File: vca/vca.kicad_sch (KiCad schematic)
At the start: 16 parts

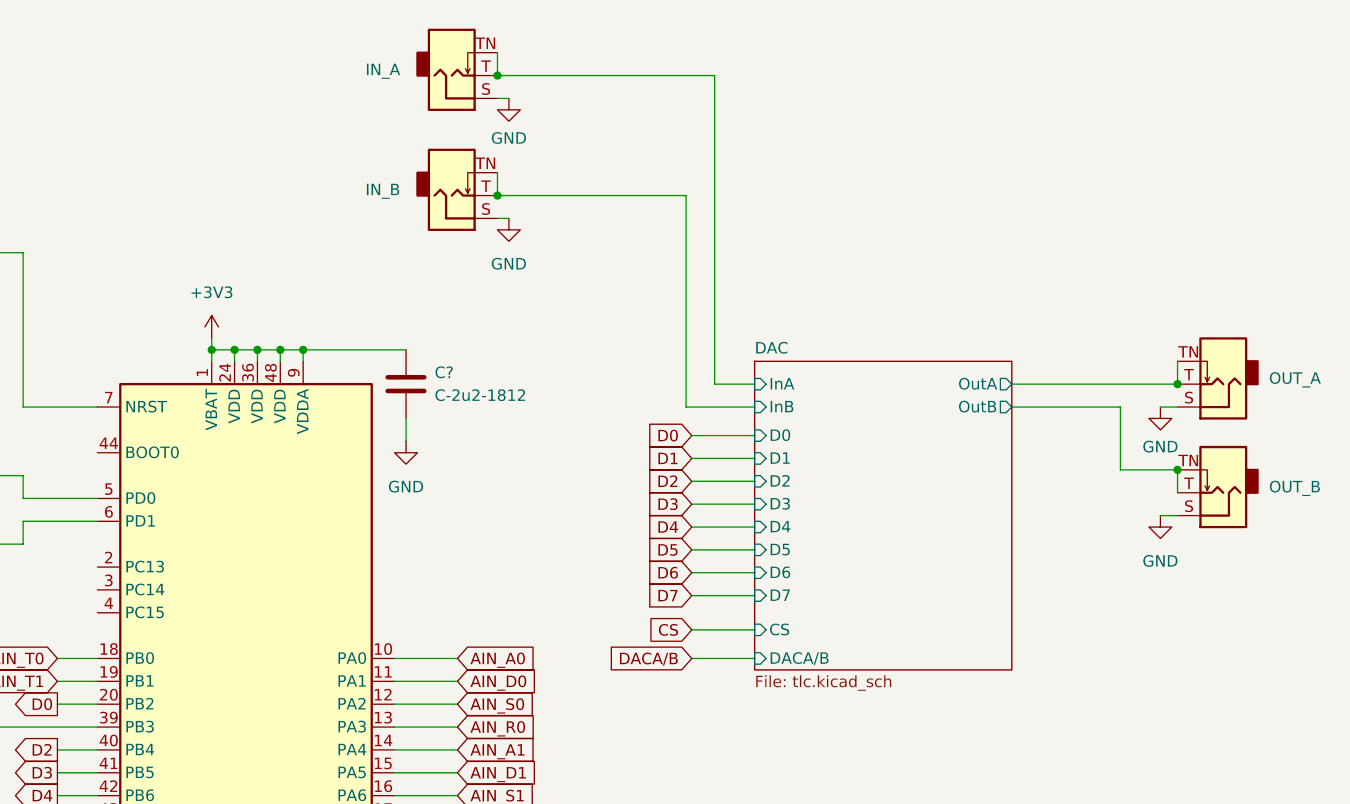
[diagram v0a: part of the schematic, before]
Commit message: added LEDs to LUM
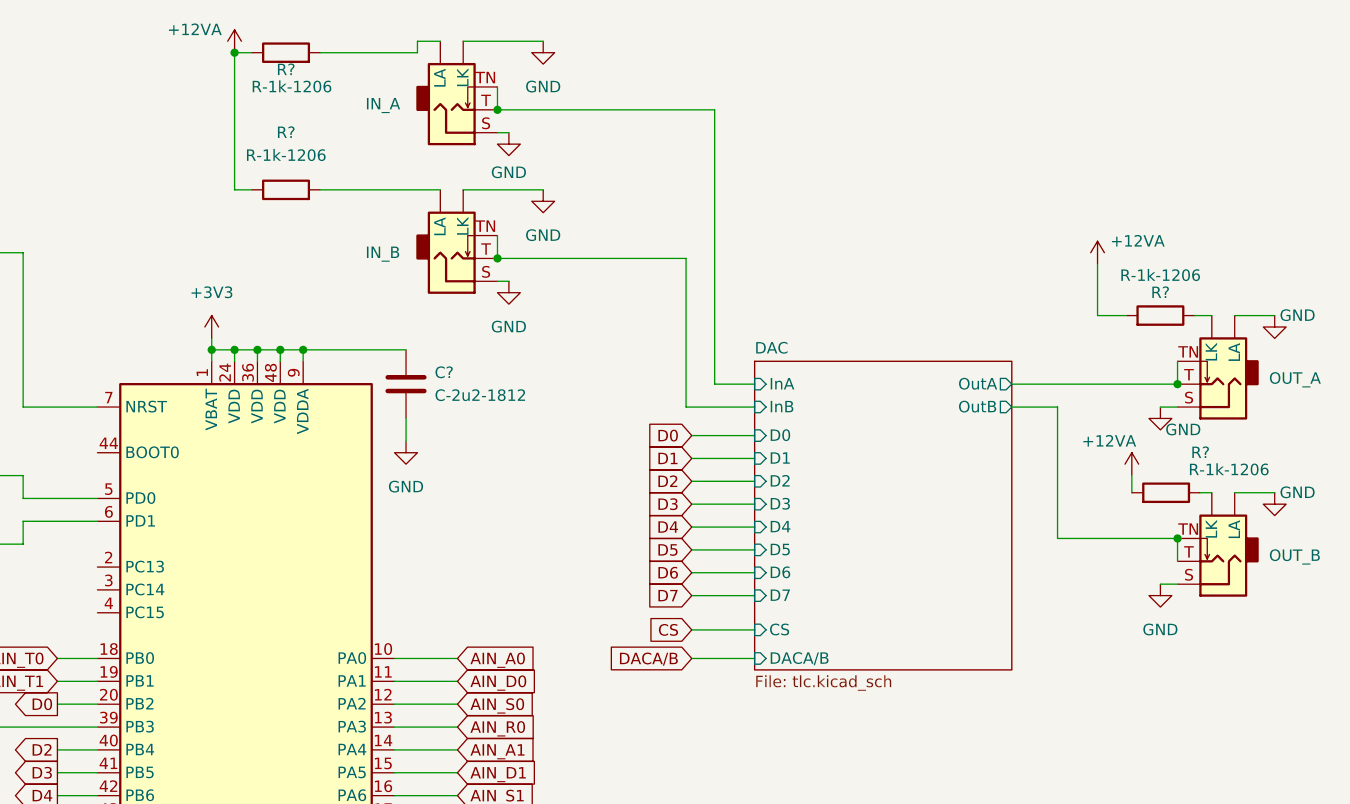
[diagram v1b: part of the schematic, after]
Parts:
- added R? (x4): R-1k-1206, Resistor_SMD:R_1206_3216Metric_Pad1.30x1.75mm_HandSolder, symbol eurorack:R-1k-1206
- IN_A, IN_B, OUT_A, OUT_B: footprint eurorack:LUM 1502-03 -> eurorack:LUM 1502-03 LED; symbol eurorack:LUM-1502-03_3.5mm_mono_vertical_jack -> eurorack:LUM-1502-03_3.5mm_mono_vertical_jack_LED
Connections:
- net GND: now also IN_A. (LK), IN_B. (LK), OUT_A. (LK), OUT_B. (LK)
- new net: OUT_B. (LK), R?.1
- new net: IN_B. (LK), R?.2
- new net: IN_A. (LK), R?.2
- new net: OUT_A. (LK), R?.1
- new net +12VA: R?.1, R?.1, R?.2, R?.2

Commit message: some fixes, starting to work on PCB
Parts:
- gave numbers to parts that had none: 16
- renumbered IN_A to IN_A1, IN_B to IN_B1, OUT_A to OUT_A1, OUT_B to OUT_B1
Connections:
- net DAC/InA: no longer IN_A1.TN
- net DAC/InB: no longer IN_B1.TN
- net GND: now also IN_A1.LK, IN_B1.LK, OUT_A1.LA, OUT_B1.LA; no longer IN_A1. (LK), IN_B1. (LK), OUT_A1. (LK), OUT_B1. (LK)
- net at R6.1: now also OUT_B1.LK; no longer OUT_B1. (LK)
- net at R4.2: now also IN_B1.LA; no longer IN_B1. (LK)
- net at R3.2: now also IN_A1.LA; no longer IN_A1. (LK)
- net at R5.1: now also OUT_A1.LK; no longer OUT_A1. (LK)
- new net +10V: IN_A1.TN

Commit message: working on the PCB
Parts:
- added CON_BACK1, CON_FRONT1: 2_15_Back_Front_Conn_70, eurorack:2_15_back_front_conn_70, symbol eurorack:2_15_Back_Front_Conn_70
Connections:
- net +10V: now also IN_B1.TN
- net AIN_A0 renamed B_AIN_A0
- net AIN_A0_LED renamed B_AIN_A0_LED
- net AIN_A1 renamed B_AIN_A1
- net AIN_A1_LED renamed B_AIN_A1_LED
- net AIN_D0 renamed B_AIN_D0
- net AIN_D0_LED renamed B_AIN_D0_LED
- net AIN_D1 renamed B_AIN_D1
- net AIN_D1_LED renamed B_AIN_D1_LED
- net AIN_R0 renamed B_AIN_R0
- net AIN_R0_LED renamed B_AIN_R0_LED
- net AIN_R1 renamed B_AIN_R1
- net AIN_R1_LED renamed B_AIN_R1_LED
- net AIN_S0 renamed B_AIN_S0
- net AIN_S0_LED renamed B_AIN_S0_LED
- net AIN_S1 renamed B_AIN_S1
- net AIN_S1_LED renamed B_AIN_S1_LED
- net AIN_T0 renamed B_AIN_T0
- net AIN_T0_LED renamed B_AIN_T0_LED
- net AIN_T1 renamed B_AIN_T1
- net AIN_T1_LED renamed B_AIN_T1_LED
- net DAC/InA renamed F_INA
- net DAC/InB renamed F_INB
- net DAC/OutA renamed F_OUTA
- net DAC/OutB renamed F_OUTB
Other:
- moved on the sheet: C4, C5, C6, C7, IN_A1, IN_B1, OUT_A1, OUT_B1, R3, R4, R5, R6

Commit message: working on front panel
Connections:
- net +10V: now also CON_FRONT1.16
- net +12VA: now also CON_FRONT1.18
- net B_AIN_R0: now also CON_BACK1.21
- net B_AIN_R0_LED: now also CON_BACK1.20
- net B_INA: now also CON_BACK1.17
- net B_INB: now also CON_BACK1.26
- net B_OUTA: now also CON_BACK1.19
- net B_OUTB: now also CON_BACK1.30
- net F_INA: now also CON_FRONT1.17
- net F_INB: now also CON_FRONT1.26
- net F_OUTA: now also CON_FRONT1.19
- net F_OUTB: now also CON_FRONT1.30
- net GND: now also OUT_A1.LK, OUT_B1.LK; no longer OUT_A1.LA, OUT_B1.LA
- net at R6.1: now also OUT_B1.LA; no longer OUT_B1.LK
- net B_+10V: now reaches CON_BACK1.16
- net +12V: now reaches CON_BACK1.18
- net at R5.1: now also OUT_A1.LA; no longer OUT_A1.LK
- net F_AIN_R0_LED: now reaches CON_FRONT1.20
- net F_AIN_R0: now reaches CON_FRONT1.21
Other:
- moved on the sheet: R5, R6

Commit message: working on the front panel
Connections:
- net +10V: now also CON_FRONT1.17; no longer CON_FRONT1.16
- net +12V: now also CON_BACK1.19; no longer CON_BACK1.18
- net +12VA: now also CON_FRONT1.19; no longer CON_FRONT1.18
- net B_+10V: now also CON_BACK1.17; no longer CON_BACK1.16
- net B_AIN_D1_LED: now also CON_BACK1.29
- net B_AIN_R0: now also CON_BACK1.23; no longer CON_BACK1.21
- net B_AIN_R0_LED: now also CON_BACK1.21; no longer CON_BACK1.20
- net B_AIN_R1: now also CON_BACK1.24
- net B_AIN_R1_LED: now also CON_BACK1.25
- net B_AIN_S0: now also CON_BACK1.16
- net B_AIN_S0_LED: now also CON_BACK1.22
- net B_AIN_S1: now also CON_BACK1.26
- net B_AIN_S1_LED: now also CON_BACK1.27
- net B_INA: now also CON_BACK1.18; no longer CON_BACK1.17
- net B_INB: now also CON_BACK1.28; no longer CON_BACK1.26
- net B_OUTA: now also CON_BACK1.20; no longer CON_BACK1.19
- net F_AIN_R0: now also CON_FRONT1.23; no longer CON_FRONT1.21
- net F_AIN_R0_LED: now also CON_FRONT1.21; no longer CON_FRONT1.20
- net F_INA: now also CON_FRONT1.18; no longer CON_FRONT1.17
- net F_INB: now also CON_FRONT1.28; no longer CON_FRONT1.26
- net F_OUTA: now also CON_FRONT1.20; no longer CON_FRONT1.19
- net F_AIN_S0_LED: now reaches CON_FRONT1.22
- net F_AIN_R1: now reaches CON_FRONT1.24
- net F_AIN_R1_LED: now reaches CON_FRONT1.25
- net F_AIN_S1_LED: now reaches CON_FRONT1.27
- net F_AIN_D1_LED: now reaches CON_FRONT1.29
- new net F_AIN_S0: CON_FRONT1.16
- new net F_AIN_S1: CON_FRONT1.26

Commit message: working on the front
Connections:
- net B_AIN_A0: now also CON_BACK1.2
- net B_AIN_A0_LED: now also CON_BACK1.6
- net B_AIN_A1: now also CON_BACK1.8
- net B_AIN_D0: now also CON_BACK1.5
- net B_AIN_D0_LED: now also CON_BACK1.7
- net B_AIN_T0: now also CON_BACK1.1
- net B_AIN_T0_LED: now also CON_BACK1.3
- net B_AIN_T1_LED: now also CON_BACK1.4
- net F_AIN_T0: now reaches CON_FRONT1.1
- net F_AIN_A0: now reaches CON_FRONT1.2
- net F_AIN_T0_LED: now reaches CON_FRONT1.3
- net F_AIN_T1_LED: now reaches CON_FRONT1.4
- net F_AIN_D0: now reaches CON_FRONT1.5
- net F_AIN_A0_LED: now reaches CON_FRONT1.6
- net F_AIN_D0_LED: now reaches CON_FRONT1.7
- net F_AIN_A1: now reaches CON_FRONT1.8

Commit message: working on the back panel power section
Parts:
- removed C10: C-2u2-1812, Capacitor_SMD:C_1812_4532Metric_Pad1.57x3.40mm_HandSolder, symbol eurorack:C-2u2-1812
- added C10: C-100nF-0805, Capacitor_SMD:C_0805_2012Metric_Pad1.18x1.45mm_HandSolder, symbol eurorack:C-100nF-0805
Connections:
- net +3V3: now also C10.1
- net B_AIN_A1_LED: now also CON_BACK1.9
- net B_AIN_T1: now also CON_BACK1.10
- net GND: now also C10.2
- net F_AIN_T1: now reaches CON_FRONT1.10
- net F_AIN_A1_LED: now reaches CON_FRONT1.9
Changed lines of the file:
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@@
+    (stroke (width 0) (type default) (color 0 0 0 0))
+  )
+  (wire (pts (xy 203.2 94.615) (xy 205.105 94.615))
     (stroke (width 0) (type default) (color 0 0 0 0))
   )
@@
     (stroke (width 0) (type default) (color 0 0 0 0))
   )
+  (wire (pts (xy 192.405 97.155) (xy 194.945 97.155))
+    (stroke (width 0) (type default) (color 0 0 0 0))
+  )
   (wire (pts (xy 203.2 89.535) (xy 205.105 89.535))
     (stroke (width 0) (type default) (color 0 0 0 0))
@@
     (stroke (width 0) (type default) (color 0 0 0 0))
   )
+  (wire (pts (xy 192.405 94.615) (xy 194.945 94.615))
+    (stroke (width 0) (type default) (color 0 0 0 0))
+  )
   (wire (pts (xy 136.525 144.145) (xy 144.78 144.145))
     (stroke (width 0) (type default) (color 0 0 0 0))
@@
     (stroke (width 0) (type default) (color 0 0 0 0))
   )
+  (wire (pts (xy 203.2 97.155) (xy 205.105 97.155))
+    (stroke (width 0) (type default) (color 0 0 0 0))
+  )
   (wire (pts (xy 203.2 122.555) (xy 205.105 122.555))
     (stroke (width 0) (type default) (color 0 0 0 0))
@@
     )
   )
+  (global_label "F_AIN_A1_LED" (shape output) (at 205.105 94.615 0) (fields_autoplaced)
+    (effects (font (size 1.27 1.27)) (justify left))
+    (property "Intersheet References" "${INTERSHEET_REFS}" (id 0) (at 220.2786 94.5356 0)
+      (effects (font (size 1.27 1.27)) (justify left) hide)
+    )
+  )
   (global_label "B_AIN_D0" (shape output) (at 192.405 84.455 180) (fields_autoplaced)
     (effects (font (size 1.27 1.27)) (justify right))
@@
     )
   )
+  (global_label "F_AIN_T1" (shape input) (at 205.105 97.155 0) (fields_autoplaced)
+    (effects (font (size 1.27 1.27)) (justify left))
+    (property "Intersheet References" "${INTERSHEET_REFS}" (id 0) (at 215.7429 97.0756 0)
+      (effects (font (size 1.27 1.27)) (justify left) hide)
+    )
+  )
   (global_label "B_AIN_T1_LED" (shape input) (at 192.405 81.915 180) (fields_autoplaced)
     (effects (font (size 1.27 1.27)) (justify right))
@@
     )
   )
+  (global_label "B_AIN_A1_LED" (shape input) (at 192.405 94.615 180) (fields_autoplaced)
+    (effects (font (size 1.27 1.27)) (justify right))
+    (property "Intersheet References" "${INTERSHEET_REFS}" (id 0) (at 177.05 94.5356 0)
+      (effects (font (size 1.27 1.27)) (justify right) hide)
+    )
+  )
   (global_label "F_AIN_D0_LED" (shape output) (at 205.105 89.535 0) (fields_autoplaced)
     (effects (font (size 1.27 1.27)) (justify left))
@@
     (property "Intersheet References" "${INTERSHEET_REFS}" (id 0) (at 219.0993 22.1456 0)
       (effects (font (size 1.27 1.27)) (justify left) hide)
+    )
+  )
+  (global_label "B_AIN_T1" (shape output) (at 192.405 97.155 180) (fields_autoplaced)
+    (effects (font (size 1.27 1.27)) (justify right))
+    (property "Intersheet References" "${INTERSHEET_REFS}" (id 0) (at 181.5857 97.0756 0)
+      (effects (font (size 1.27 1.27)) (justify right) hide)
     )
   )
@@
     )
     (property "Datasheet" "https://secure.reichelt.com/at/en/smd-multilayer-ceramic-capacitor-100-n-10--x7r-g0805-100n-p31879.html?&nbc=1" (id 3) (at 160.655 147.955 0)
+      (effects (font (size 1.27 1.27)) hide)
+    )
+    (pin "1")
+    (pin "2")
+  )
+  (symbol (lib_id "eurorack:C-100nF-0805") (at 139.065 53.34 0) (unit 1)
+    (in_bom yes) (on_board yes) (fields_autoplaced)
+    (property "Reference" "C10" (id 0) (at 142.875 52.0699 0)
+      (effects (font (size 1.27 1.27)) (justify left))
+    )
+    (property "Value" "C-100nF-0805" (id 1) (at 142.875 54.6099 0)
+      (effects (font (size 1.27 1.27)) (justify left))
+    )
+    (property "Footprint" "Capacitor_SMD:C_0805_2012Metric_Pad1.18x1.45mm_HandSolder" (id 2) (at 140.0302 57.15 0)
+      (effects (font (size 1.27 1.27)) hide)
+    )
+    (property "Datasheet" "https://secure.reichelt.com/at/en/smd-multilayer-ceramic-capacitor-100-n-10--x7r-g0805-100n-p31879.html?&nbc=1" (id 3) (at 139.065 53.34 0)
       (effects (font (size 1.27 1.27)) hide)
     )
@@
     )
     (pin "1")
-  )
-  (symbol (lib_id "eurorack:C-2u2-1812") (at 139.065 53.34 0) (unit 1)
-    (in_bom yes) (on_board yes) (fields_autoplaced)
-    (property "Reference" "C10" (id 0) (at 142.24 52.0699 0)
-      (effects (font (size 1.27 1.27)) (justify left))
-    )
-    (property "Value" "C-2u2-1812" (id 1) (at 142.24 54.6099 0)
-      (effects (font (size 1.27 1.27)) (justify left))
-    )
-    (property "Footprint" "Capacitor_SMD:C_1812_4532Metric_Pad1.57x3.40mm_HandSolder" (id 2) (at 140.0302 57.15 0)
-      (effects (font (size 1.27 1.27)) hide)
-    )
-    (property "Datasheet" "https://secure.reichelt.com/at/en/mlcc-1812-2-2-f-100-v-10--ecc-kts101b225k-p256478.html?search=2.2+uF&&r=1" (id 3) (at 139.065 53.34 0)
-      (effects (font (size 1.27 1.27)) hide)
-    )
-    (pin "1")
-    (pin "2")
   )
   (symbol (lib_id "power:GND") (at 139.065 59.69 0) (unit 1)
@@
       (reference "C9") (unit 1) (value "15pF") (footprint "Capacitor_SMD:C_1206_3216Metric_Pad1.33x1.80mm_HandSolder")
     )
-    (path "/a0cc1b01-bcab-4e05-9afc-fd0a7f1f6228"
-      (reference "C10") (unit 1) (value "C-2u2-1812") (footprint "Capacitor_SMD:C_1812_4532Metric_Pad1.57x3.40mm_HandSolder")
+    (path "/36318a3a-84ac-444d-ae85-6f6cf0299141"
+      (reference "C10") (unit 1) (value "C-100nF-0805") (footprint "Capacitor_SMD:C_0805_2012Metric_Pad1.18x1.45mm_HandSolder")
     )
     (path "/91f87fc6-c431-4dbd-bf9a-22d85a993784/f4147ca2-5f1b-4675-996b-57876e945f91"
